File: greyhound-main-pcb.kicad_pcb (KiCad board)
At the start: 4 copper layers, 84 x 78 mm, 280 parts, among them J1 Conn_01x03, J10 Conn_01x02, J11 Conn_01x06, J12 Conn_01x03, J13 613012243121, J16 2x20_P2.54mm_Pinheader, J17 Conn_01x03, J18 2x20_P2.54mm_Pinheader, J19 Conn_01x02, J2 Conn_01x03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

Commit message: Remove 1V8 LDO
Signed-off-by: Leo Moser <leomoser99@gmail.com>
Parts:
- removed C11: 1uF, Capacitor_SMD:C_0603_1608Metric
- removed C13: 100nF, Capacitor_SMD:C_0402_1005Metric
- removed C7: 10uF, Capacitor_SMD:C_0805_2012Metric
- removed D3: Yellow, LED_SMD:LED_0603_1608Metric
- removed J19: Conn_01x02, Connector_PinHeader_2.54mm:PinHeader_1x02_P2.54mm_Vertical
- removed Q1: DMN2005K, Package_TO_SOT_SMD:SOT-23
- removed R18: 510, Resistor_SMD:R_0402_1005Metric
- removed R49: 0R, Resistor_SMD:R_0603_1608Metric
- removed R50: 47R, Resistor_SMD:R_0402_1005Metric
- removed U3: AP2112K-1.8, Package_TO_SOT_SMD:SOT-23-5
- added ?: , , F.Cu at (112.8, 61.9)
- added ?: , , F.Cu at (115.0, 55.4)
- added ?: , , F.Cu at (115.5, 60.5)
- moved D2 3.75 mm to (139.5, 57.2)
- moved R17 3.75 mm to (138.2, 56.6)
- moved D1 1.85 mm to (145.9, 57.2)
- moved R15 1.85 mm to (144.7, 56.6)
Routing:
- net +1V8: track 28.4 -> 0.00 mm
- net +3V3: track 651.0 -> 639.5 mm, vias 53 -> 52
- net /1v8A: track 9.79 -> 0.00 mm
- net GND: track 84.9 -> 76.6 mm, vias 68 -> 63
- net Net-(D3-K): track 5.19 -> 0.00 mm, vias 2 -> 0
- net +5V: track 56.7 -> 54.3 mm
- net Net-(Q1-G): track 2.25 -> 0.00 mm
- net Net-(D3-A): track 1.43 -> 0.00 mm
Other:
- board text removed: "1V8"

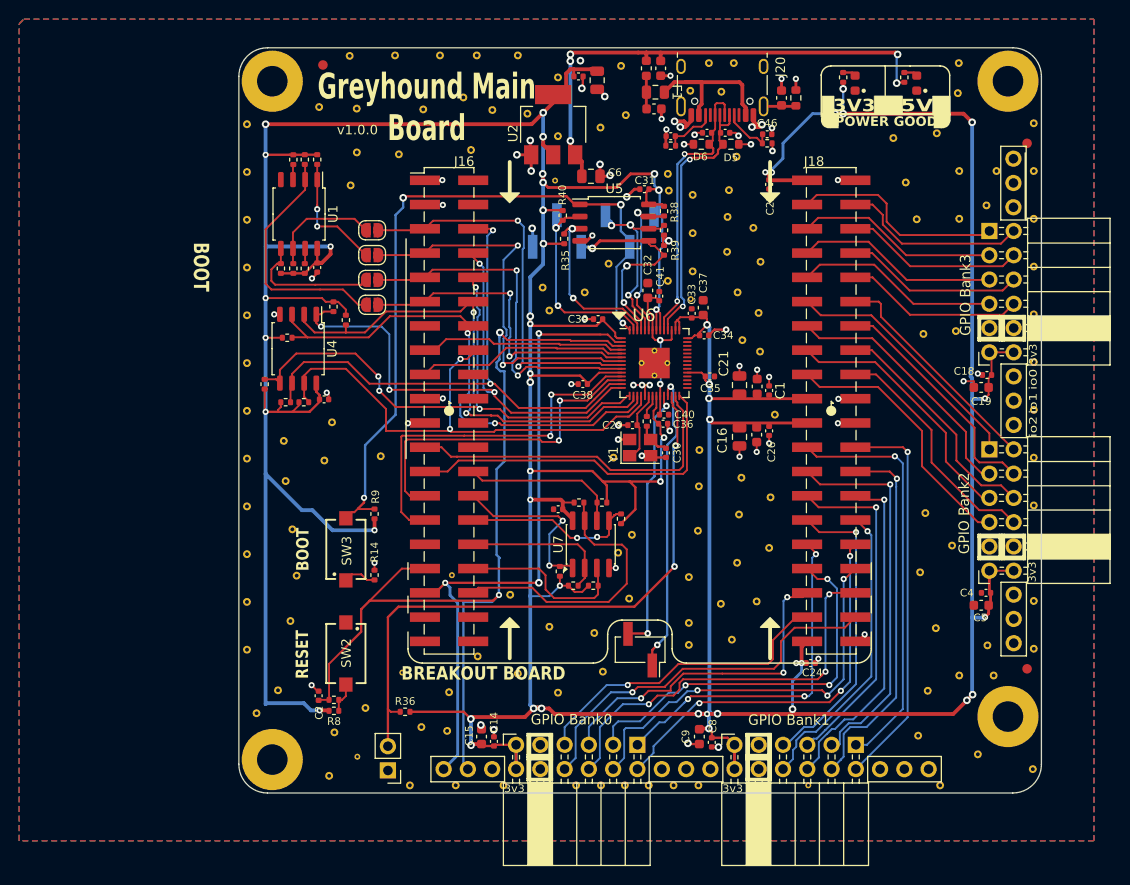
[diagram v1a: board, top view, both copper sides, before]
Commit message: Update README, add images
Signed-off-by: Leo Moser <leomoser99@gmail.com>
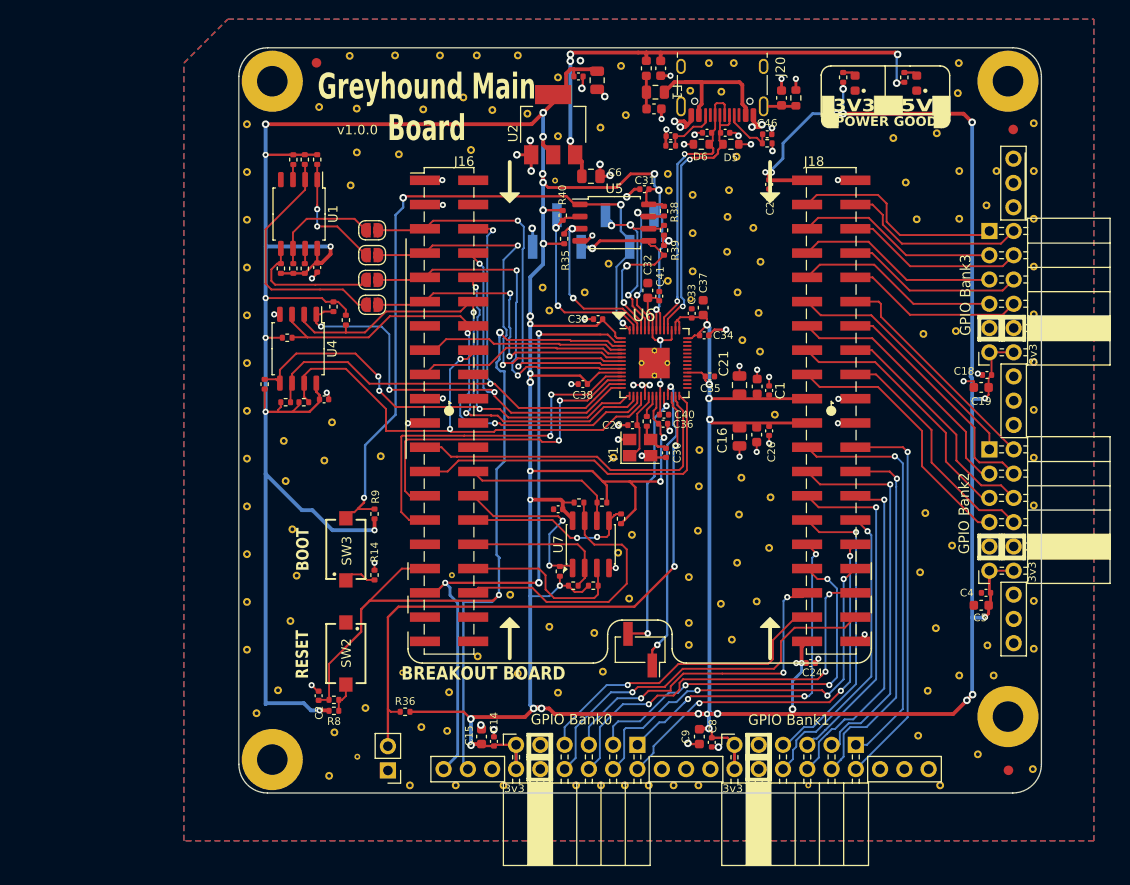
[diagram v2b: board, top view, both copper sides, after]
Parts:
- moved FID1 10.8 mm to (155.6, 129.1)
- moved FID3 2.05 mm to (156.1, 62.0)
- moved FID2 0.71 mm to (83.1, 55.1)
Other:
- board text removed: "BIDIR"
- board text removed: "CLK"
- board text removed: "CTRL"
- board text removed: "OUTPUT"
- board text removed: "io0"
- board text removed: "io1"
- board text removed: "io2"
- board text removed: "io3"
- board text removed: "io4"
- board text removed: "io5"
- board text removed: "io6"
- board text removed: "io7"
- board text removed: "o0"
- board text removed: "o1"
- board text removed: "o2"
- board text removed: "o3"
- board text removed: "o4"
- board text removed: "o5"
- board text removed: "o6"
- board text removed: "o7"
- board text removed: "uio"
- board text removed: "uo_out"
- board text removed: "~{RST}"

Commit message: Move resistor
Signed-off-by: Leo Moser <leomoser99@gmail.com>
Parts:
- moved R11 2.29 mm to (77.8, 84.2), turned to -90 degrees
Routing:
- net /FLASH_IO2: track 54.1 -> 57.2 mm
- net +3V3: track 639.5 -> 638.9 mm
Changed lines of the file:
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@@
 	(footprint "Resistor_SMD:R_0402_1005Metric"
 		(layer "F.Cu")
-		(at 80.06 83.85)
+		(at 77.8 84.2 -90)
 		(descr "Resistor SMD 0402 (1005 Metric), square (rectangular) end terminal, IPC-7351 nominal, (Body size source: IPC-SM-782 page 72, https://www.pcb-3d.com/wordpress/wp-content/uploads/ipc-sm-782a_amendment_1_and_2.pdf), generated with kicad-footprint-generator")
 		(tags "resistor")
 		(property "Reference" "R11"
-			(at 0 -1.17 0)
+			(at 0 -1.17 90)
 			(layer "F.SilkS")
 			(hide yes)
@@
 		)
 		(property "Value" "10k"
-			(at 0 1.17 0)
+			(at 0 1.17 90)
 			(layer "F.Fab")
 			(effects
@@
 		)
 		(property "Datasheet" "~"
-			(at 0 0 0)
+			(at 0 0 90)
 			(layer "F.Fab")
 			(hide yes)
@@
 		)
 		(property "Description" ""
-			(at 0 0 0)
+			(at 0 0 90)
 			(layer "F.Fab")
 			(hide yes)
@@
 		)
 		(property "MPN" "RC0402FR-0710KL"
-			(at 0 0 0)
+			(at 0 0 270)
 			(unlocked yes)
 			(layer "F.Fab")
@@
 		)
 		(property "Characteristics" "10k 0402"
-			(at 0 0 0)
+			(at 0 0 270)
 			(unlocked yes)
 			(layer "F.Fab")
@@
 		)
 		(property "MPN_ALT" "WR04X1002FTL"
-			(at 0 0 0)
+			(at 0 0 270)
 			(unlocked yes)
 			(layer "F.Fab")
@@
 		)
 		(property "MANUFACTURER" ""
-			(at 0 0 0)
+			(at 0 0 270)
 			(unlocked yes)
 			(layer "F.Fab")
@@
 		)
 		(property "MAXIMUM_PACKAGE_HEIGHT" ""
-			(at 0 0 0)
+			(at 0 0 270)
 			(unlocked yes)
 			(layer "F.Fab")
@@
 		)
 		(property "LCSC" "C471764"
-			(at 0 0 0)
+			(at 0 0 270)
 			(unlocked yes)
 			(layer "F.Fab")
@@
 		(attr smd)
 		(fp_line
-			(start -0.153641 -0.38)
-			(end 0.153641 -0.38)
+			(start -0.153641 0.38)
+			(end 0.153641 0.38)
 			(stroke
 				(width 0.12)
@@
 		)
 		(fp_line
-			(start -0.153641 0.38)
-			(end 0.153641 0.38)
+			(start -0.153641 -0.38)
+			(end 0.153641 -0.38)
 			(stroke
 				(width 0.12)
@@
 		)
 		(fp_text user "${REFERENCE}"
-			(at 0 0 0)
+			(at 0 0 90)
 			(layer "F.Fab")
 			(effects
@@
 		)
 		(pad "1" smd roundrect
-			(at -0.51 0)
+			(at -0.51 0 270)
 			(size 0.54 0.64)
 			(layers "F.Cu" "F.Mask" "F.Paste")
@@
 		)
 		(pad "2" smd roundrect
-			(at 0.51 0)
+			(at 0.51 0 270)
 			(size 0.54 0.64)
 			(layers "F.Cu" "F.Mask" "F.Paste")
@@
 	)
 	(segment
-		(start 79.55 83.85)
-		(end 77.8 83.85)
-		(width 0.2)
-		(layer "F.Cu")
-		(net 3)
-	)
-	(segment
 		(start 123.82 87.9)
 		(end 123.82 88.310254)
@@
 	)
 	(segment
+		(start 77.8 83.69)
+		(end 77.8 82.525)
+		(width 0.2)
+		(layer "F.Cu")
+		(net 3)
+	)
+	(segment
 		(start 150.85 60.4)
 		(end 137.4 60.4)
@@
 	)
 	(via
-		(at 77.8 83.85)
+		(at 77.8 82.525)
 		(size 0.65)
 		(drill 0.3)
@@
 	)
 	(segment
+		(start 80.62 83.8)
+		(end 82.165001 83.8)
+		(width 0.2)
+		(layer "F.Cu")
+		(net 88)
+	)
+	(segment
+		(start 82.165001 83.8)
+		(end 82.175001 83.81)
+		(width 0.2)
+		(layer "F.Cu")
+		(net 88)
+	)
+	(segment
+		(start 77.8 84.71)
+		(end 79.71 84.71)
+		(width 0.2)
+		(layer "F.Cu")
+		(net 88)
+	)
+	(segment
 		(start 99.525 82.61)
 		(end 99.525 82.798)
@@
 	)
 	(segment
+		(start 79.71 84.71)
+		(end 80.62 83.8)
+		(width 0.2)
+		(layer "F.Cu")
+		(net 88)
+	)
+	(segment
 		(start 116.7 90.679942)
 		(end 115.739971 91.639971)
@@
 	)
 	(segment
-		(start 80.57 83.85)
-		(end 80.62 83.8)
-		(width 0.2)
-		(layer "F.Cu")
-		(net 88)
-	)
-	(segment
 		(start 116.7 89.9375)
 		(end 116.7 90.679942)
@@
 	)
 	(segment
-		(start 80.62 83.8)
-		(end 82.165001 83.8)
-		(width 0.2)
-		(layer "F.Cu")
-		(net 88)
-	)
-	(segment
 		(start 112.079942 93)
 		(end 102.5 93)
@@
 		(width 0.2)
 		(layer "F.Cu")
-		(net 88)
-	)
-	(segment
-		(start 82.165001 83.8)
-		(end 82.175001 83.81)
-		(width 0.2)
-		(layer "F.Cu")
